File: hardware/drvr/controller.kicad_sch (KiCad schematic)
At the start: 0 parts

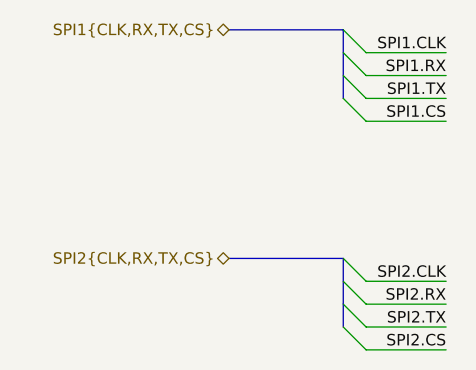
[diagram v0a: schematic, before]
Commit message: added initial gate-drive design
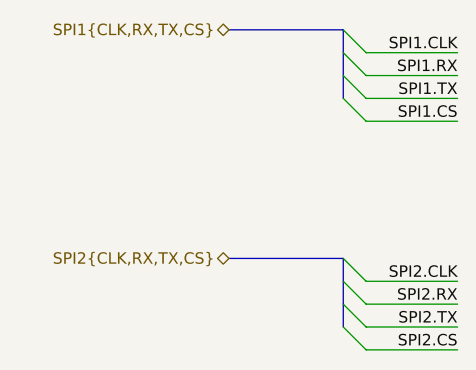
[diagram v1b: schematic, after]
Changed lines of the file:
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@@
 	(wire
 		(pts
-			(xy 76.2 60.96) (xy 67.31 60.96)
-		)
-		(stroke
-			(width 0)
-			(type default)
-		)
-	)
-	(wire
-		(pts
-			(xy 76.2 55.88) (xy 67.31 55.88)
+			(xy 77.47 60.96) (xy 67.31 60.96)
+		)
+		(stroke
+			(width 0)
+			(type default)
+		)
+	)
+	(wire
+		(pts
+			(xy 77.47 55.88) (xy 67.31 55.88)
 		)
 		(stroke
@@
 	(wire
 		(pts
-			(xy 76.2 83.82) (xy 67.31 83.82)
-		)
-		(stroke
-			(width 0)
-			(type default)
-		)
-	)
-	(wire
-		(pts
-			(xy 76.2 86.36) (xy 67.31 86.36)
+			(xy 77.47 83.82) (xy 67.31 83.82)
+		)
+		(stroke
+			(width 0)
+			(type default)
+		)
+	)
+	(wire
+		(pts
+			(xy 77.47 86.36) (xy 67.31 86.36)
 		)
 		(stroke
@@
 	(wire
 		(pts
-			(xy 76.2 78.74) (xy 67.31 78.74)
-		)
-		(stroke
-			(width 0)
-			(type default)
-		)
-	)
-	(wire
-		(pts
-			(xy 76.2 58.42) (xy 67.31 58.42)
+			(xy 77.47 78.74) (xy 67.31 78.74)
+		)
+		(stroke
+			(width 0)
+			(type default)
+		)
+	)
+	(wire
+		(pts
+			(xy 77.47 58.42) (xy 67.31 58.42)
 		)
 		(stroke
@@
 	(wire
 		(pts
-			(xy 76.2 53.34) (xy 67.31 53.34)
-		)
-		(stroke
-			(width 0)
-			(type default)
-		)
-	)
-	(wire
-		(pts
-			(xy 76.2 81.28) (xy 67.31 81.28)
+			(xy 77.47 53.34) (xy 67.31 53.34)
+		)
+		(stroke
+			(width 0)
+			(type default)
+		)
+	)
+	(wire
+		(pts
+			(xy 77.47 81.28) (xy 67.31 81.28)
 		)
 		(stroke
@@
 	)
 	(label "SPI2.CLK"
-		(at 76.2 78.74 180)
+		(at 77.47 78.74 180)
 		(effects
 			(font
@@
 	)
 	(label "SPI1.CS"
-		(at 76.2 60.96 180)
+		(at 77.47 60.96 180)
 		(effects
 			(font
@@
 	)
 	(label "SPI1.CLK"
-		(at 76.2 53.34 180)
+		(at 77.47 53.34 180)
 		(effects
 			(font
@@
 	)
 	(label "SPI2.RX"
-		(at 76.2 81.28 180)
+		(at 77.47 81.28 180)
 		(effects
 			(font
@@
 	)
 	(label "SPI1.RX"
-		(at 76.2 55.88 180)
+		(at 77.47 55.88 180)
 		(effects
 			(font
@@
 	)
 	(label "SPI2.TX"
-		(at 76.2 83.82 180)
+		(at 77.47 83.82 180)
 		(effects
 			(font
@@
 	)
 	(label "SPI1.TX"
-		(at 76.2 58.42 180)
+		(at 77.47 58.42 180)
 		(effects
 			(font
@@
 	)
 	(label "SPI2.CS"
-		(at 76.2 86.36 180)
-		(effects
-			(font
+		(at 77.47 86.36 180)
+		(effects
+			(font

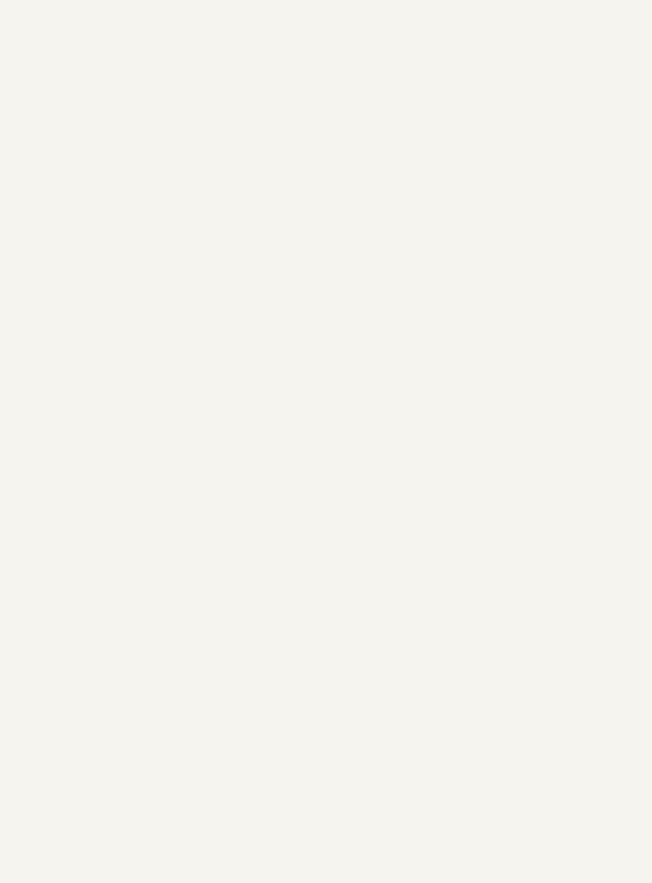
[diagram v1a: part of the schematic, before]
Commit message: added gatedrivers + pico as draft
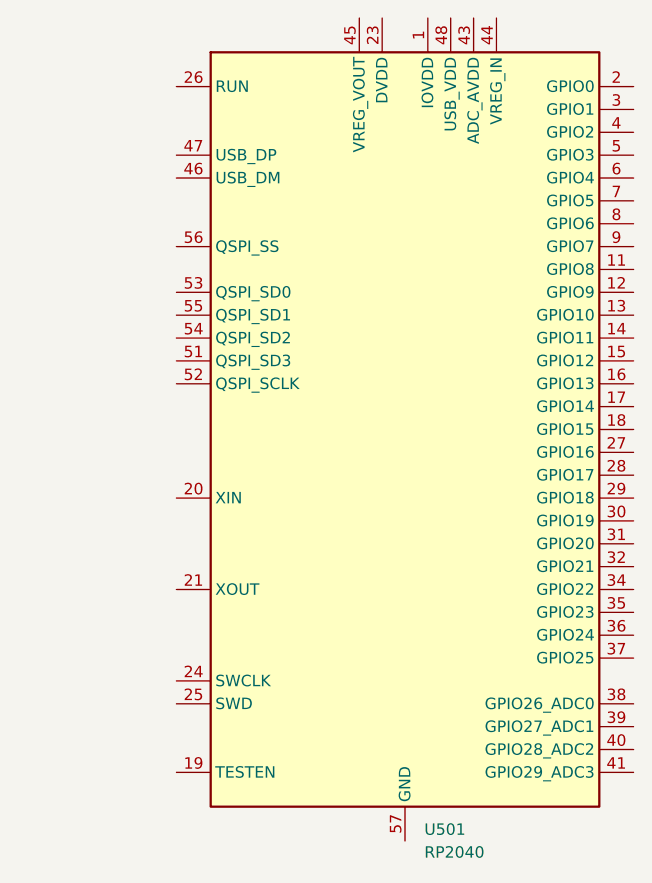
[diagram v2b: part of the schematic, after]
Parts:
- added U501: RP2040, Package_DFN_QFN:QFN-56-1EP_7x7mm_P0.4mm_EP3.2x3.2mm, symbol MCU_RaspberryPi:RP2040
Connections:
- new net: U501.1 (IOVDD), U501.10 (IOVDD), U501.22 (IOVDD), U501.33 (IOVDD), U501.42 (IOVDD), U501.49 (IOVDD)
- new net: U501.23 (DVDD), U501.50 (DVDD)
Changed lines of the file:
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@@
+		)
+	)
+	(symbol
+		(lib_id "MCU_RaspberryPi:RP2040")
+		(at 161.29 92.71 0)
+		(unit 1)
+		(exclude_from_sim no)
+		(in_bom yes)
+		(on_board yes)
+		(dnp no)
+		(fields_autoplaced yes)
+		(property "Reference" "U501"
+			(at 163.4333 137.16 0)
+			(effects
+				(font
+					(size 1.27 1.27)
+				)
+				(justify left)
+			)
+		)
+		(property "Value" "RP2040"
+			(at 163.4333 139.7 0)
+			(effects
+				(font
+					(size 1.27 1.27)
+				)
+				(justify left)
+			)
+		)
+		(property "Footprint" "Package_DFN_QFN:QFN-56-1EP_7x7mm_P0.4mm_EP3.2x3.2mm"
+			(at 161.29 92.71 0)
+			(effects
+				(font
+					(size 1.27 1.27)
+				)
+				(hide yes)
+			)
+		)
+		(property "Datasheet" "https://datasheets.raspberrypi.com/rp2040/rp2040-datasheet.pdf"
+			(at 161.29 92.71 0)
+			(effects
+				(font
+					(size 1.27 1.27)
+				)
+				(hide yes)
+			)
+		)
+		(property "Description" "A microcontroller by Raspberry Pi"
+			(at 161.29 92.71 0)
+			(effects
+				(font
+					(size 1.27 1.27)
+				)
+				(hide yes)
+			)
+		)
+		(pin "20"
+		)
+		(pin "56"
+		)
+		(pin "51"
+		)
+		(pin "54"
+		)
+		(pin "21"
+		)
+		(pin "15"
+		)
+		(pin "16"
+		)
+		(pin "17"
+		)
+		(pin "18"
+		)
+		(pin "25"
+		)
+		(pin "53"
+		)
+		(pin "27"
+		)
+		(pin "28"
+		)
+		(pin "29"
+		)
+		(pin "30"
+		)
+		(pin "31"
+		)
+		(pin "32"
+		)
+		(pin "34"
+		)
+		(pin "35"
+		)
+		(pin "36"
+		)
+		(pin "37"
+		)
+		(pin "38"
+		)
+		(pin "39"
+		)
+		(pin "40"
+		)
+		(pin "41"
+		)
+		(pin "10"
+		)
+		(pin "22"
+		)
+		(pin "33"
+		)
+		(pin "42"
+		)
+		(pin "23"
+		)
+		(pin "50"
+		)
+		(pin "57"
+		)
+		(pin "1"
+		)
+		(pin "2"
+		)
+		(pin "3"
+		)
+		(pin "4"
+		)
+		(pin "5"
+		)
+		(pin "49"
+		)
+		(pin "48"
+		)
+		(pin "43"
+		)
+		(pin "44"
+		)
+		(pin "6"
+		)
+		(pin "7"
+		)
+		(pin "8"
+		)
+		(pin "9"
+		)
+		(pin "11"
+		)
+		(pin "12"
+		)
+		(pin "13"
+		)
+		(pin "14"
+		)
+		(pin "19"
+		)
+		(pin "45"
+		)
+		(pin "26"
+		)
+		(pin "47"
+		)
+		(pin "46"
+		)
+		(pin "52"
+		)
+		(pin "24"
+		)
+		(pin "55"
+		)
+		(instances
+			(project ""
+				(path "/81ae36e8-9cac-4279-b747-86fcffa363b5/ac48ce9a-62aa-464c-b4b8-a7c8fd6ab1a5"
+					(reference "U501")
+					(unit 1)
+				)
+			)
 		)
 	)
